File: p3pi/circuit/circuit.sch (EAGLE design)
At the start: 22 parts, among them IC1 TS 5205 CX533, Q1 BSS123, X1 STECKER_MICROMATCH_4SMD, X2 STECKER_MICROMATCH_4SMD

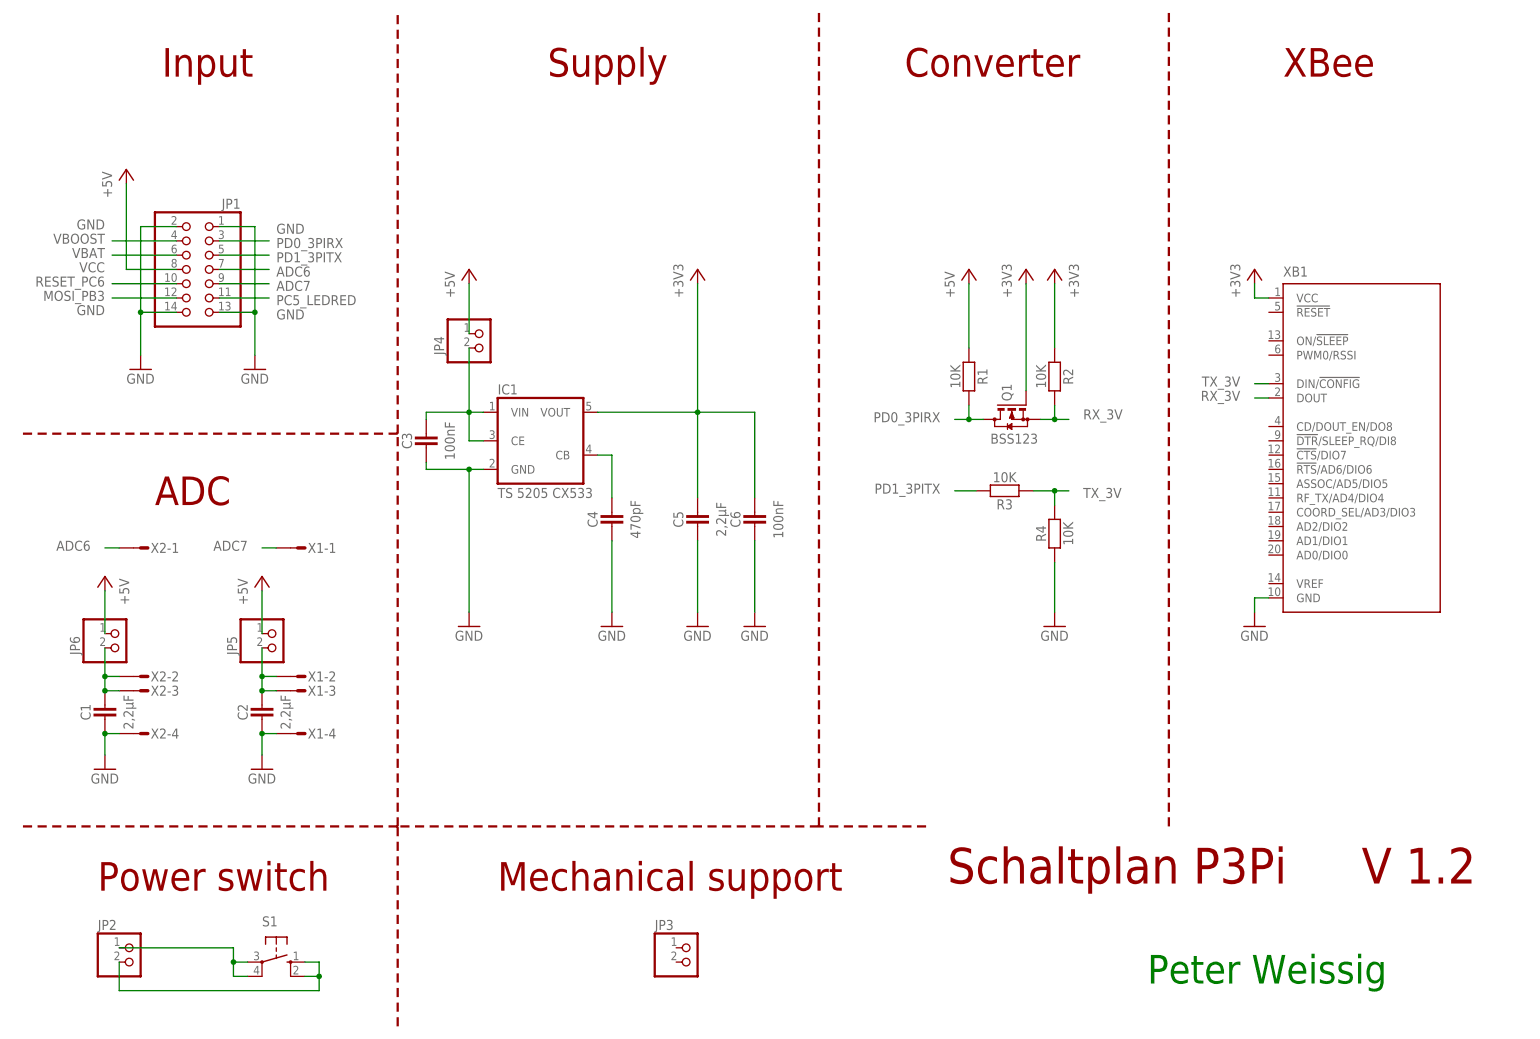
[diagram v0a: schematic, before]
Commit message: update P3Pi to Version 1.3
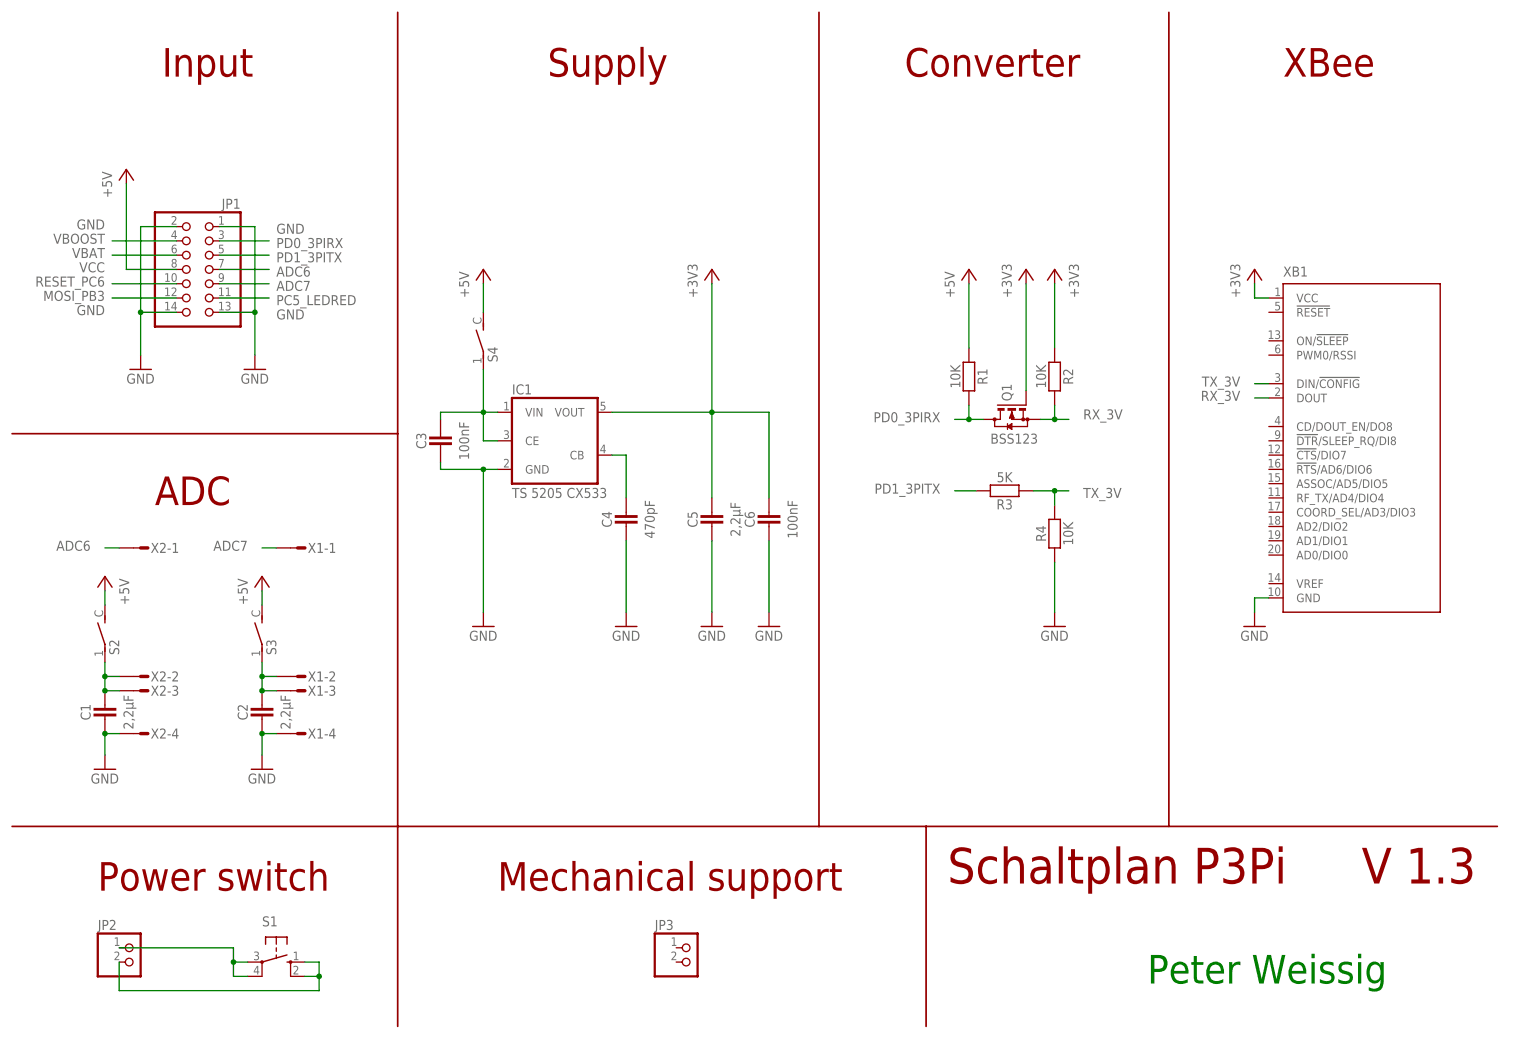
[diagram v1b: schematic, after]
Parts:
- removed JP4, JP5, JP6: (no value), pinhead:PINHD-1X2
- added S2, S3, S4: (no value), robo_ag:SCHALTER
- R3: value 10K -> 5K
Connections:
- net VCC: now also S2.2, S3.2, S4.2; no longer JP4.1, JP5.1, JP6.1
- net VCC_ADC6: now also S2.1; no longer JP6.2
- net VCC_ADC7: now also S3.1; no longer JP5.2
- net VCC_XBEE: now also S4.1; no longer JP4.2
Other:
- note added: "V 1.3"
- note removed: "V 1.2"
- moved on the sheet: C3, C4, C5, C6, IC1
